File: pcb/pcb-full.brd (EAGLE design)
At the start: 127 x 76.2 mm, 127 parts, among them IC1 STM32F401RET6U, IC2 LDS3985M33R, IC3 LDS3985M33R, IC4 HX711, IC5 TLV2462IP, J12 B2B-PH-K-S_LF__SN_, J14 3V3 LED, J15 VDDA LED, J16 HX711 LED, J18 DC Power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

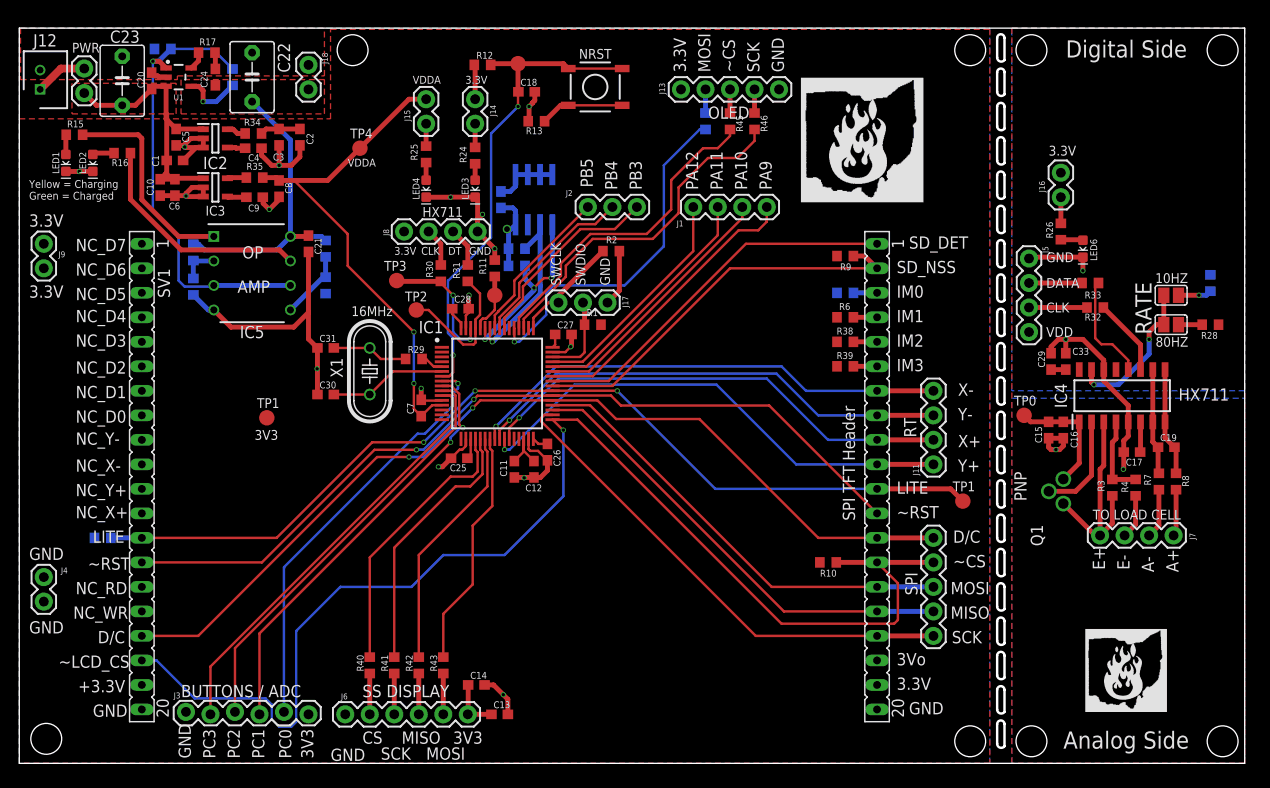
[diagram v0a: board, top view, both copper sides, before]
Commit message: Updated the 8 mil trace clearance and DRC
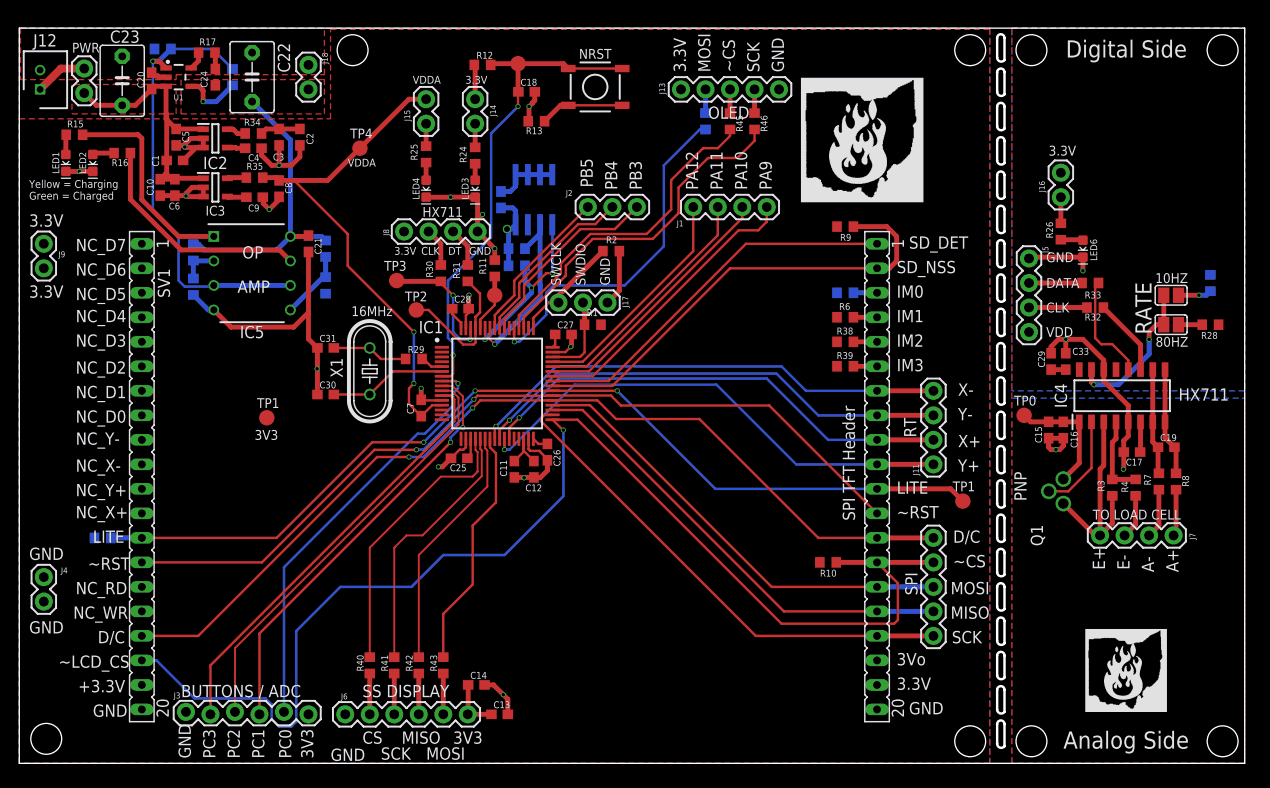
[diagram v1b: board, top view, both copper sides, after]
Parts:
- moved R9 3.05 mm to (85.6, 55.6)
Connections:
- net D0 renamed D0_NC
- net D1 renamed D1_NC
- net D2 renamed D2_NC
- net D3 renamed D3_NC
- net D4 renamed D4_NC
- net D5 renamed D5_NC
- net D6 renamed D6_NC
- net D7 renamed D7_NC
- net RD renamed RD_NC
- net WR renamed WR_NC
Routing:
- net SD_CS: track 41.7 -> 48.5 mm
- net _SS_CS: track 28.7 -> 29.3 mm
- net MEM_SCL: track 33.0 -> 33.5 mm

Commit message: Final version of the PCB? Updated headers + silkscreen + AGND
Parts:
- added R47: 0.1, LinnesLab-Passives:R0603
- J3: device LinnesLab-Connectors:1X06_LOCK -> LinnesLab-Connectors:1X06
- moved U$9 0.76 mm to (81.8, 58.2)
- moved C18 0.51 mm to (52.6, 70.1)
- moved R36 0.25 mm to (51.6, 53.1)
- moved R37 0.25 mm to (51.6, 51.3)
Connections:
- net GND-ISO: now also R47.1, R47.2
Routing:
- net GND-ISO: track 38.0 -> 80.0 mm, vias 4 -> 6
- net GND: track 122.4 -> 122.9 mm
- added copper zone on layer 1, net NC
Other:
- board text added: "5V"
- board text added: "B"
- board text added: "C"
- board text added: "E"
- board text added: "I2C EEPROM"
- board text added: "LED"
- board text added: "LiPo"
- board text added: "Team 10: Smart Ingredient Scale Ryan Montsma - Hardware Engineer Gautam Fotedar - Systems Engineer Jeremy Tang - Team Leader Ben Schwartz - Software Engineer Board Revision 1.0"
- board text removed: "CS"
- board text removed: "Team 10: Smart Ingredient Scale Jeremy Tang - Team Leader Gautam Fotedar - Systems Engineer Ben Schwartz - Software Engineer Ryan Montsma - Hardware Engineer Board Revision 1.0"

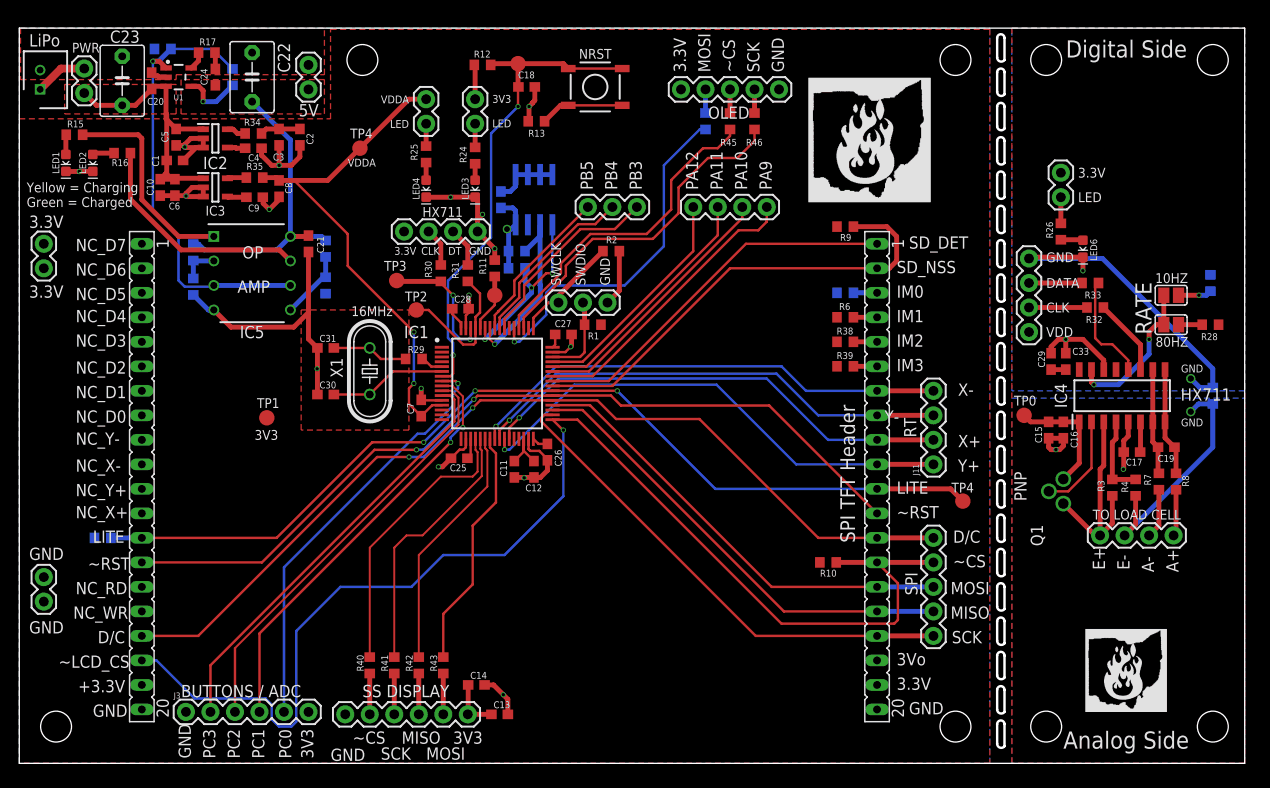
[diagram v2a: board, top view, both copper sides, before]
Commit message: Finished updating the PCB + Gerber files zip file
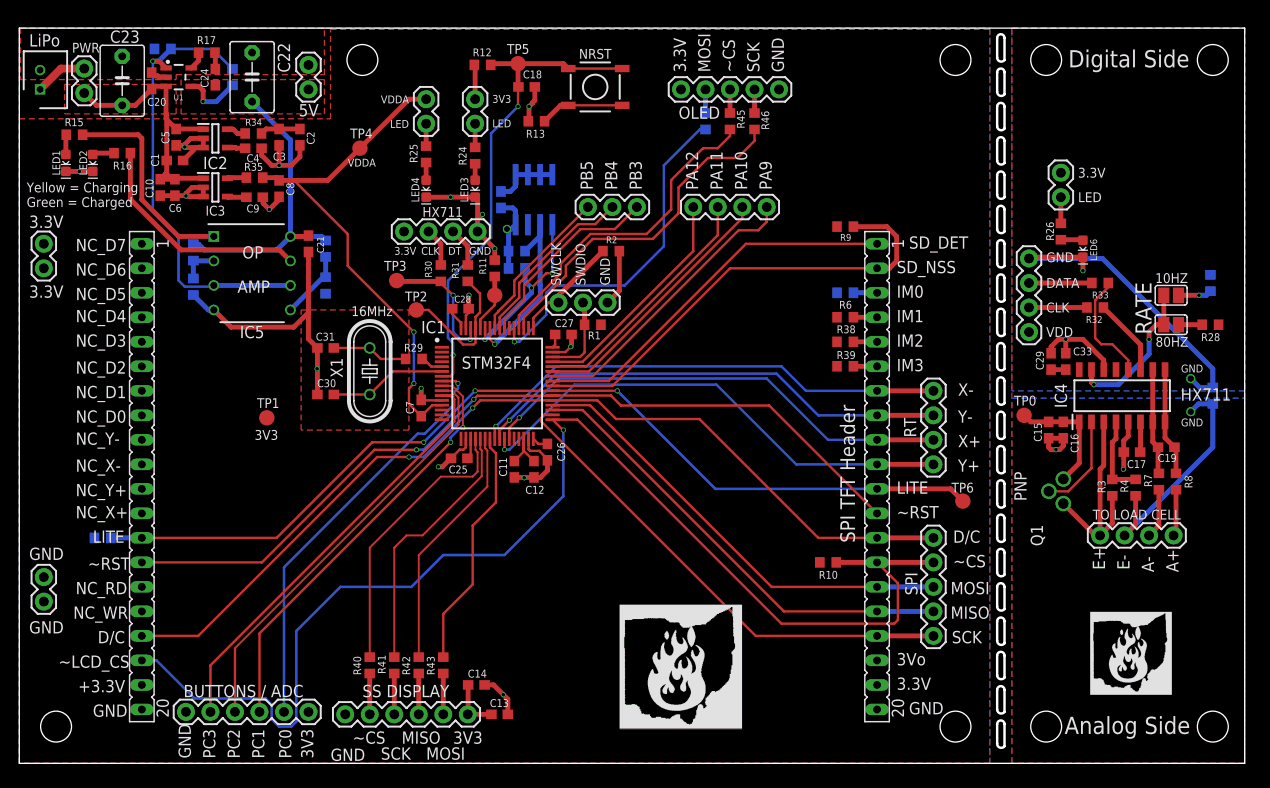
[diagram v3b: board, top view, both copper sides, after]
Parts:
- moved U$9 58.0 mm to (62.2, 3.56)
- moved U$10 1.85 mm to (111.0, 7.11)
- moved R33 1.02 mm to (112.0, 49.8)
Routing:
- net _HXDATA: track 5.50 -> 6.52 mm
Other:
- board text added: "AGND Solder Bridge"
- board text added: "Ryan Montsma - Hardware Engineer Gautam Fotedar - Systems Engineer Jeremy Tang - Team Leader Ben Schwartz - Software Engineer Board Revision 1.0"
- board text added: "STM32F4"
- board text added: "TP5"
- board text added: "TP6"
- board text added: "Team 10: Smart Ingredient Scale"
- board text removed: "Team 10: Smart Ingredient Scale Ryan Montsma - Hardware Engineer Gautam Fotedar - Systems Engineer Jeremy Tang - Team Leader Ben Schwartz - Software Engineer Board Revision 1.0"
